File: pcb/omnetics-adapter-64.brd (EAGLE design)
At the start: 19 x 9 mm, 9 parts, among them J1 DF40-REC

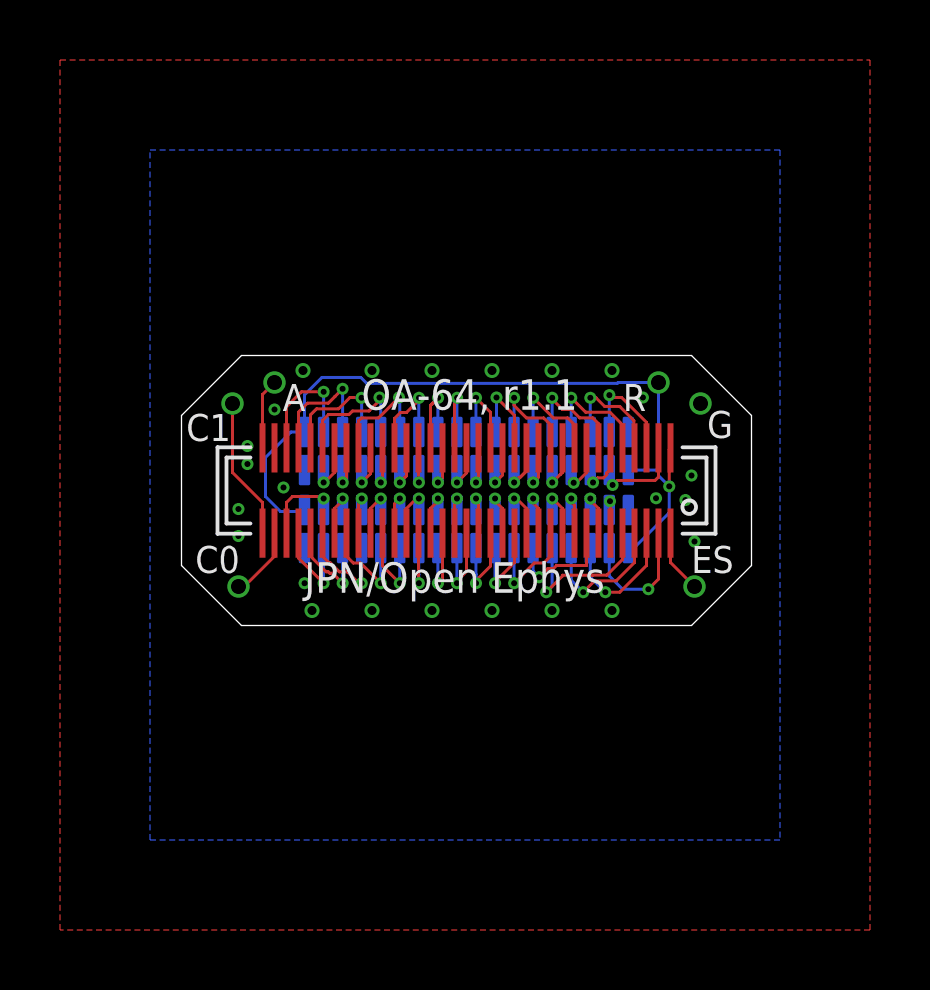
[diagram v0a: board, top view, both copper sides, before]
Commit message: Replace design with 1.3 pinout
- This pinout fits headstage-64 that is in the field
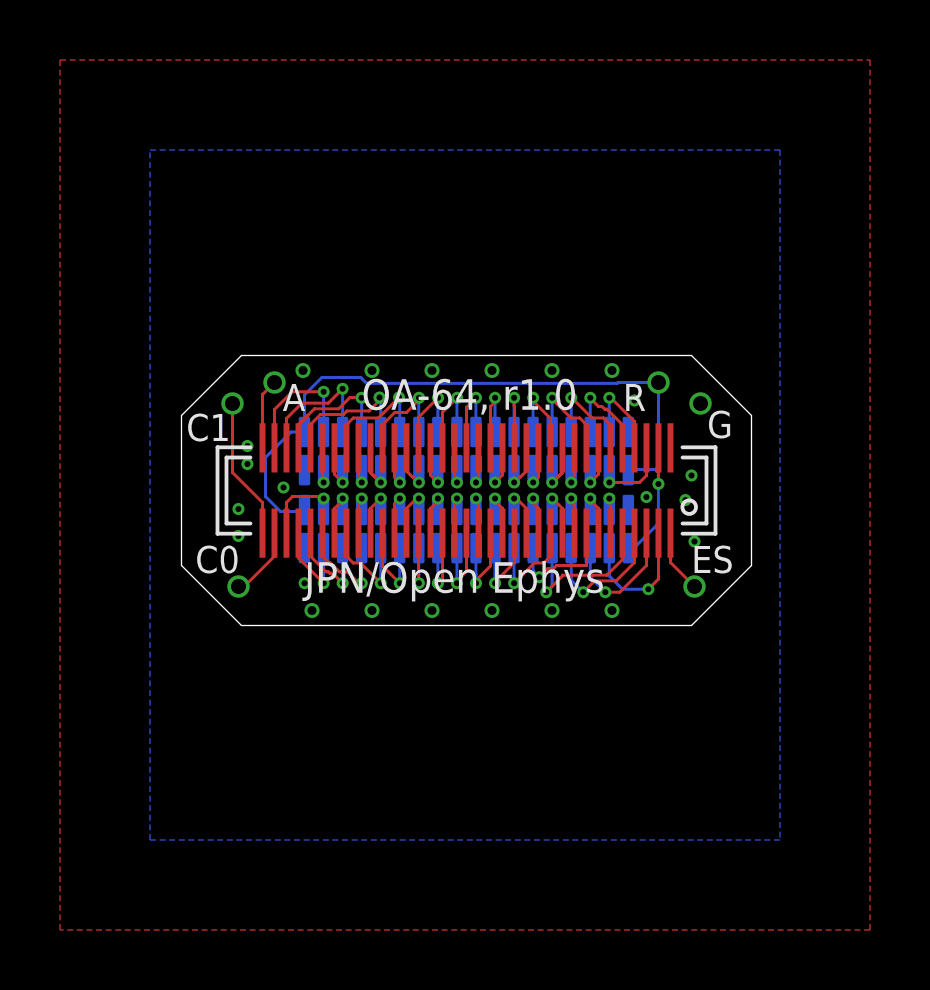
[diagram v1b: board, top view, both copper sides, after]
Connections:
- net GND: now also J1.70; no longer J1.37
- net N$1: now also J1.68; no longer J1.69
- net N$12: now also J1.57; no longer J1.60
- net N$14: now also J1.55; no longer J1.57
- net N$16: now also J1.53; no longer J1.55
- net N$17: now also J1.52; no longer J1.53
- net N$18: now also J1.51; no longer J1.52
- net N$19: now also J1.50; no longer J1.51
- net N$2: now also J1.65; no longer J1.66
- net N$20: now also J1.49; no longer J1.50
- net N$21: now also J1.48; no longer J1.49
- net N$22: now also J1.47; no longer J1.48
- net N$23: now also J1.46; no longer J1.47
- net N$24: now also J1.45; no longer J1.46
- net N$25: now also J1.44; no longer J1.45
- net N$26: now also J1.43; no longer J1.44
- net N$27: now also J1.42; no longer J1.43
- net N$28: now also J1.41; no longer J1.42
- net N$29: now also J1.40; no longer J1.41
- net N$3: now also J1.66; no longer J1.67
- net N$30: now also J1.39; no longer J1.40
- net N$31: now also J1.38; no longer J1.39
- net N$32: now also J1.37; no longer J1.38
- net N$4: now also J1.67; no longer J1.68
- net N$5: now also J1.64; no longer J1.65
- net N$6: now also J1.63; no longer J1.64
- net N$7: now also J1.62; no longer J1.63
- net N$9: now also J1.60; no longer J1.62
- net REF: now also J1.69; no longer J1.70
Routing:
- net N$28: track 1.73 -> 3.48 mm
- net N$21: track 1.57 -> 3.21 mm
- net N$24: track 1.59 -> 2.81 mm
- net N$23: track 3.27 -> 4.32 mm
- net N$8: track 1.82 -> 2.81 mm
- net N$29: track 4.36 -> 5.26 mm
- net N$16: track 3.78 -> 2.94 mm
- net N$12: track 3.65 -> 2.82 mm
- net N$13: track 1.67 -> 2.49 mm
- net N$17: track 1.70 -> 2.47 mm
- net N$31: track 4.43 -> 5.18 mm
- net N$9: track 3.77 -> 3.05 mm
- net N$25: track 1.69 -> 2.38 mm
- net N$30: track 4.19 -> 4.85 mm
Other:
- board text added: "OA-64, r1.0"
- board text removed: "OA-64, r1.1"
